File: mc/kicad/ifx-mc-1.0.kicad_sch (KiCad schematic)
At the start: 37 parts, among them J2 FTSH-105-01-H-DV-K-TR, J3 XT30PW-F, Q1 IRLR7843, Q2 IRLR7843, Q3 IRLR7843, Q4 IRLR7843, SW1 SKRPABE010, U1 CY8C4146LQI-S422, U2 XT30UPB-M, U3 IR2184S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

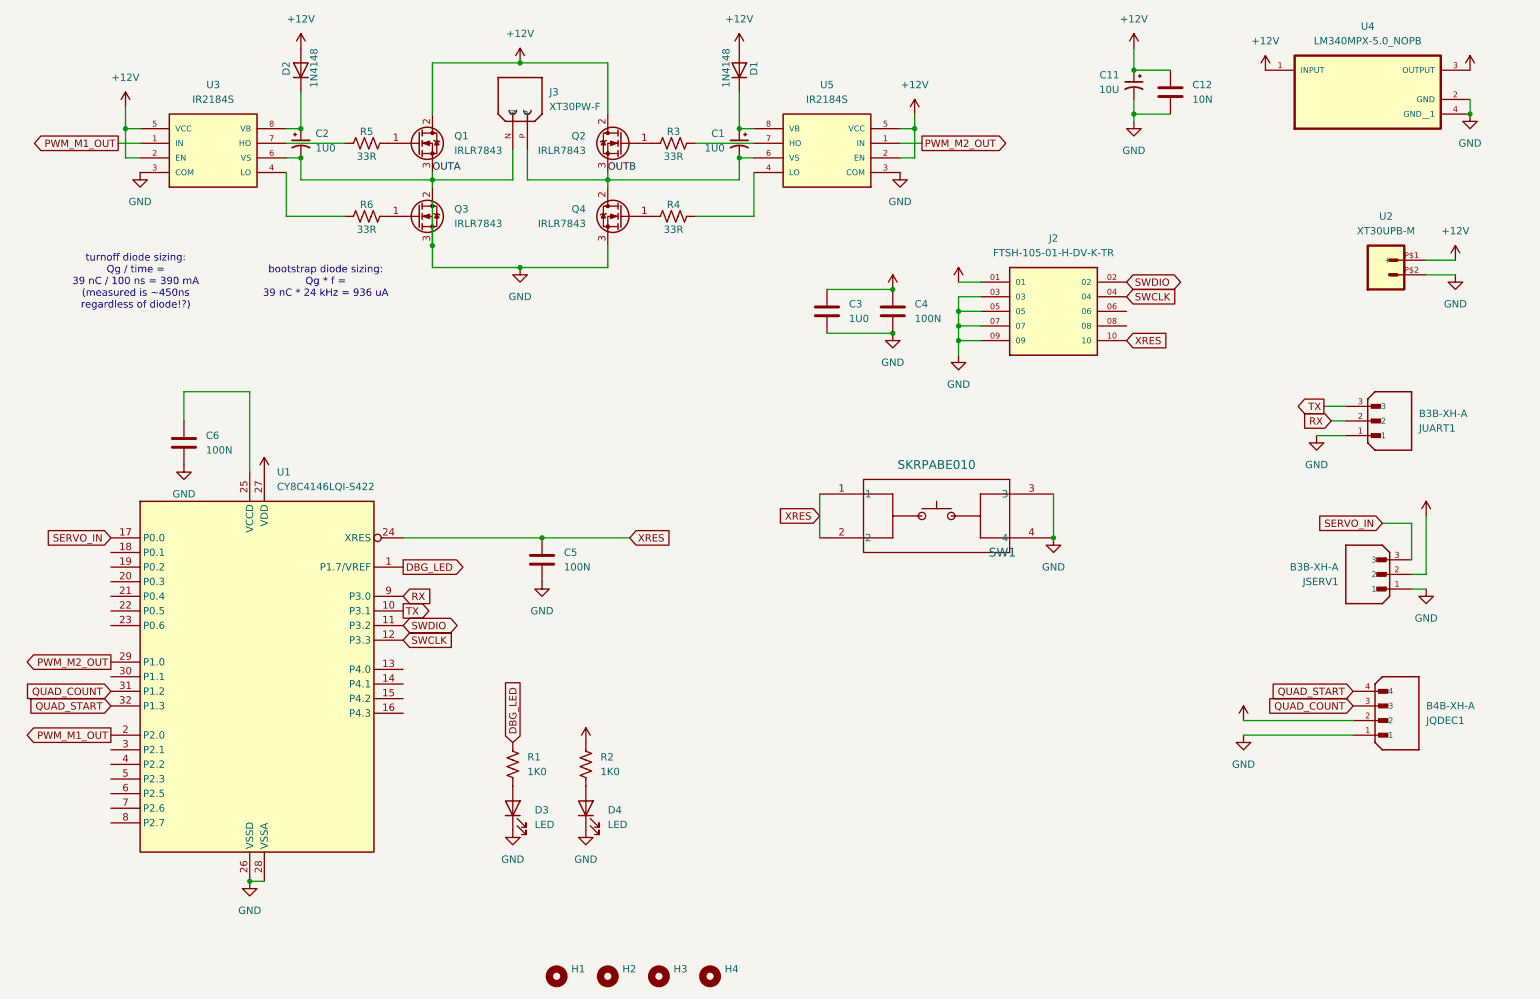
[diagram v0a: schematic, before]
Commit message: Annoted wiring issue on JQDEC1
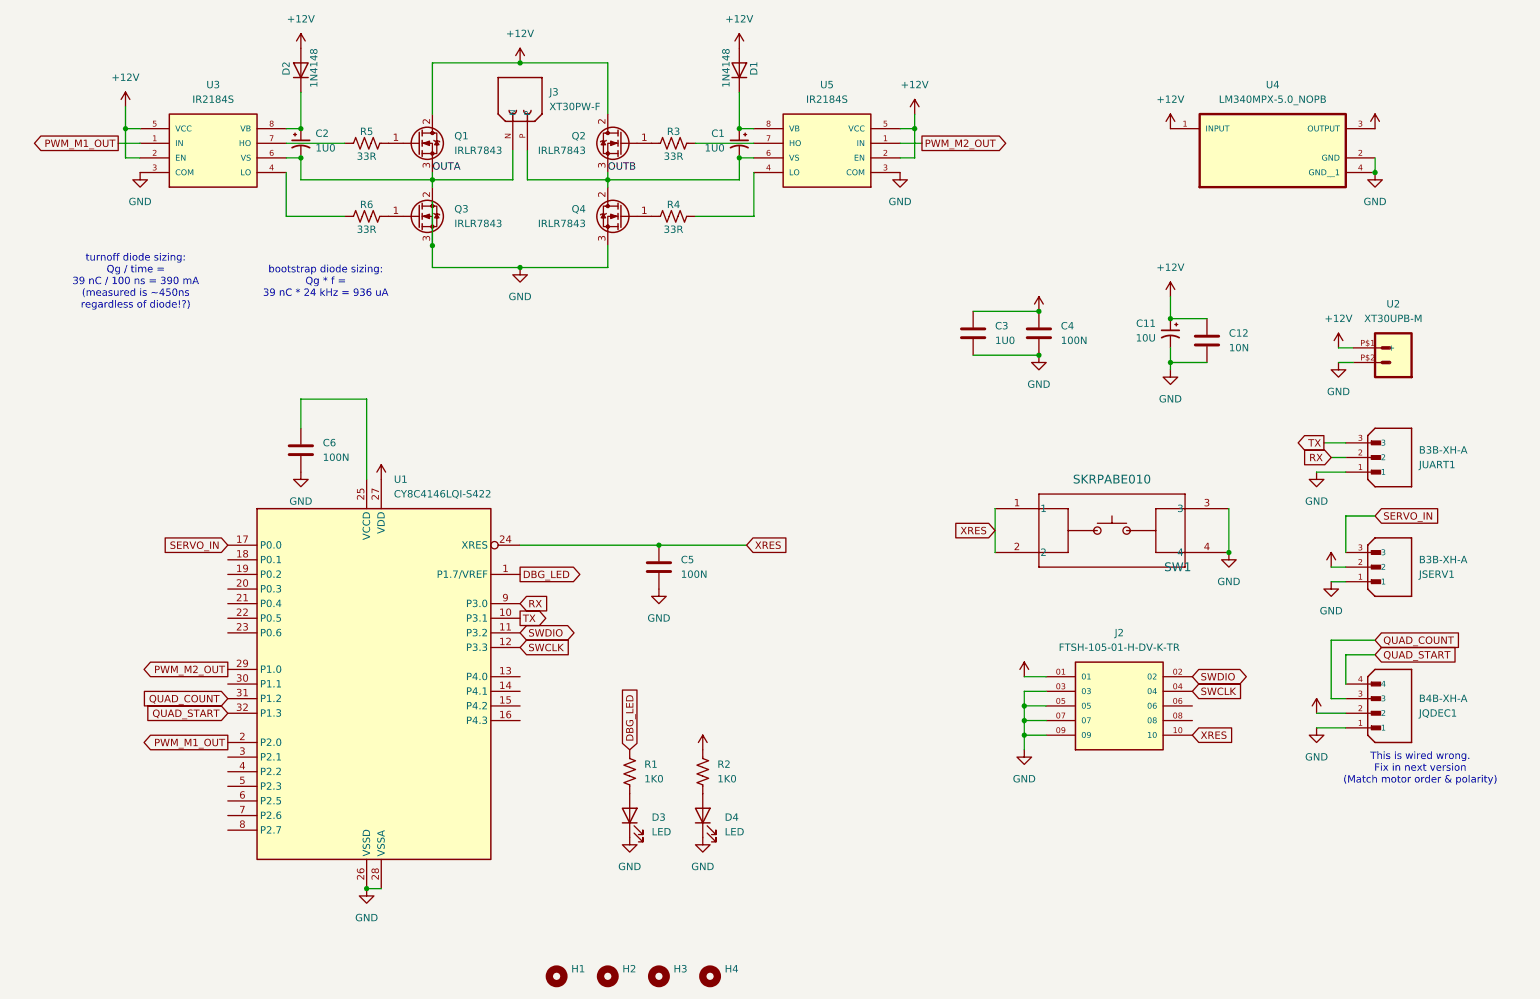
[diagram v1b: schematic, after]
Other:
- note added: "This is wired wrong. Fix in next version (Match motor order & polarity)"
- moved on the sheet: C11, C12, C3, C4, C5, C6, D3, D4, J2, JQDEC1, JSERV1, JUART1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
